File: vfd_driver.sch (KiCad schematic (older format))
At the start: 32 parts, among them J1 Input, J2 futaba_7_lt_44z, J3 High Volt, J4 FIL_n, J5 FIL_p, Q3 BC817, Q4 BC807, Q5 BC817, Q6 BC807, U2 74HC595, U3 74HC595, U4 74HC595, U5 TBD62783A, U6 TBD62783A, U7 TBD62783A

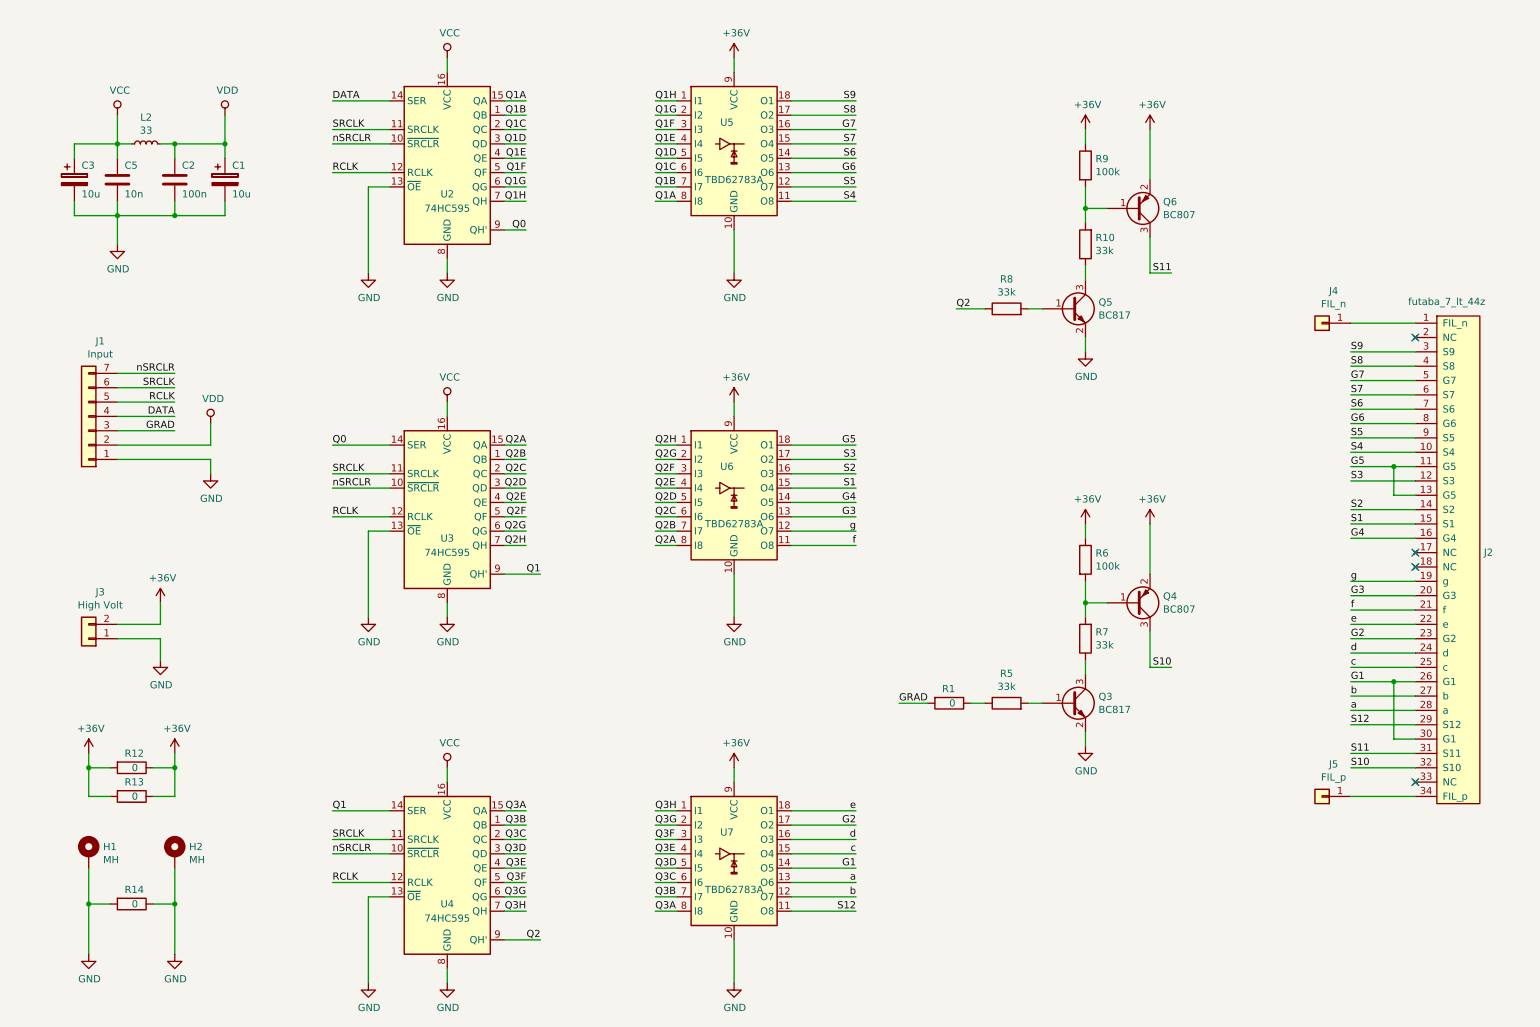
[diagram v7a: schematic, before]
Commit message: Power and logic are separated and working well.
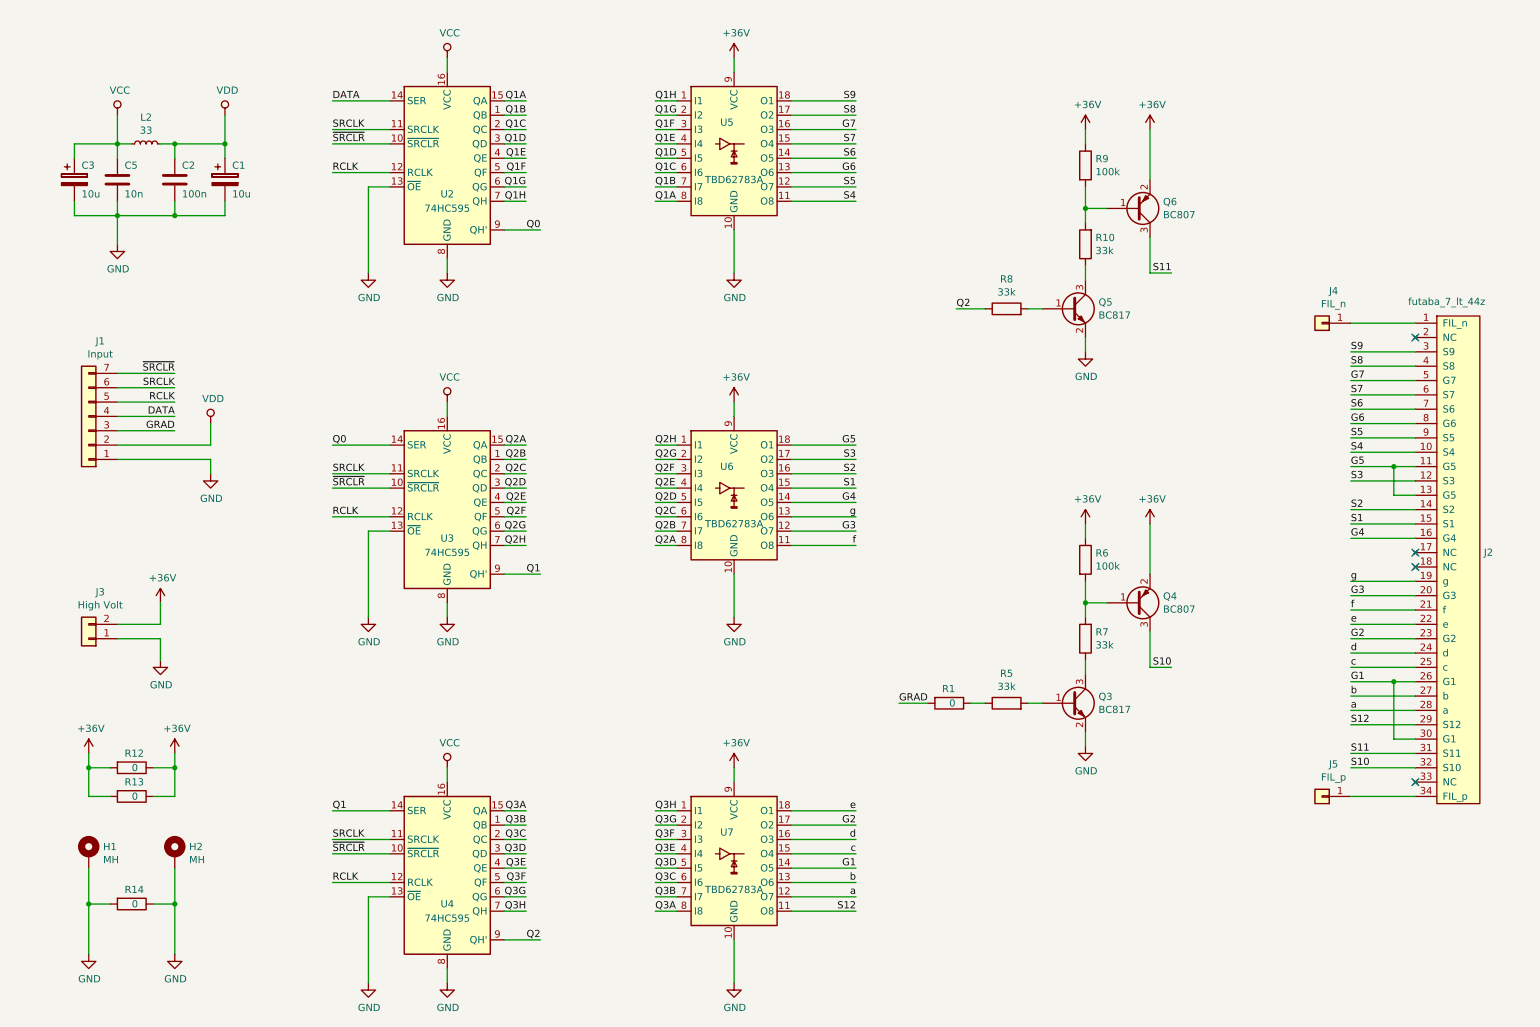
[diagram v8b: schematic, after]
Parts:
- J2: footprint Connector_PinSocket_2.54mm:PinSocket_1x34_P2.54mm_Vertical_SMD_Pin1Left -> Connector_PinSocket_2.54mm:PinSocket_1x34_P2.54mm_Vertical
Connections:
- net G3: now also U6.12 (O7); no longer U6.13 (O6)
- net a: now also U7.12 (O7); no longer U7.13 (O6)
- net b: now also U7.13 (O6); no longer U7.12 (O7)
- net g: now also U6.13 (O6); no longer U6.12 (O7)
- net nSRCLR renamed ~SRCLR
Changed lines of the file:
@@
 encoding utf-8
 Sheet 1 1
-Title ""
+Title "VFD DRIVER"
 Date ""
 Rev ""
@@
 SRCLK
 Text Label 2800 1500 0    50   ~ 0
-nSRCLR
+~SRCLR
 Text Label 2800 1700 0    50   ~ 0
 RCLK
@@
 F 0 "J2" H 10828 4351 50  0000 L CNN
 F 1 "futaba_7_lt_44z" H 10300 6100 50  0000 L CNN
-F 2 "Connector_PinSocket_2.54mm:PinSocket_1x34_P2.54mm_Vertical_SMD_Pin1Left" H 10550 4350 50  0001 C CNN
+F 2 "Connector_PinSocket_2.54mm:PinSocket_1x34_P2.54mm_Vertical" H 10550 4350 50  0001 C CNN
 F 3 "" H 10550 4350 50  0001 C CNN
 	1    10550 4350
@@
 NoConn ~ 10350 4450
 NoConn ~ 10350 5950
-Text Label 4150 2100 2    50   ~ 0
+Text Label 4250 2100 2    50   ~ 0
 Q0
 Wire Wire Line
@@
 SRCLK
 Text Label 2800 3900 0    50   ~ 0
-nSRCLR
+~SRCLR
 Text Label 2800 4100 0    50   ~ 0
 RCLK
@@
 SRCLK
 Text Label 2800 6450 0    50   ~ 0
-nSRCLR
+~SRCLR
 Text Label 2800 6650 0    50   ~ 0
 RCLK
@@
 Text Label 6450 3700 2    50   ~ 0
 S3
-Text Label 6450 4100 2    50   ~ 0
+Text Label 6450 4200 2    50   ~ 0
 G3
 Text Label 6450 4000 2    50   ~ 0
@@
 Text Label 6450 3600 2    50   ~ 0
 G5
-Text Label 6450 4200 2    50   ~ 0
+Text Label 6450 4100 2    50   ~ 0
 g
 Text Label 6450 4300 2    50   ~ 0
@@
 Text Label 6450 6450 2    50   ~ 0
 c
+Text Label 6450 6650 2    50   ~ 0
+b
 Text Label 6450 6750 2    50   ~ 0
-b
-Text Label 6450 6650 2    50   ~ 0
 a
 Wire Wire Line
@@
 $EndComp
 Text Label 1700 3100 2    50   ~ 0
-nSRCLR
+~SRCLR
 Wire Wire Line
 	1700 3100 1300 3100
@@
 Wire Wire Line
 	1000 2000 1300 2000
-Wire Wire Line
-	4150 2100 4000 2100
 $Comp
 L Connector_Generic:Conn_01x01 J4
@@
 Wire Wire Line
 	7250 5400 7350 5400
+Wire Wire Line
+	4000 2100 4250 2100
 $EndSCHEMATC
